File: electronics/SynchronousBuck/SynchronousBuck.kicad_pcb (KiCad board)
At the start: 4 copper layers, 90 x 81 mm, 58 parts, among them J101 Conn_01x02, J102 Conn_01x04_Male, J103 Conn_01x02, J104 Conn_01x02, Q101 BSC070N10NS5, Q102 BSC067N06LS3G, U101 LM5116MH

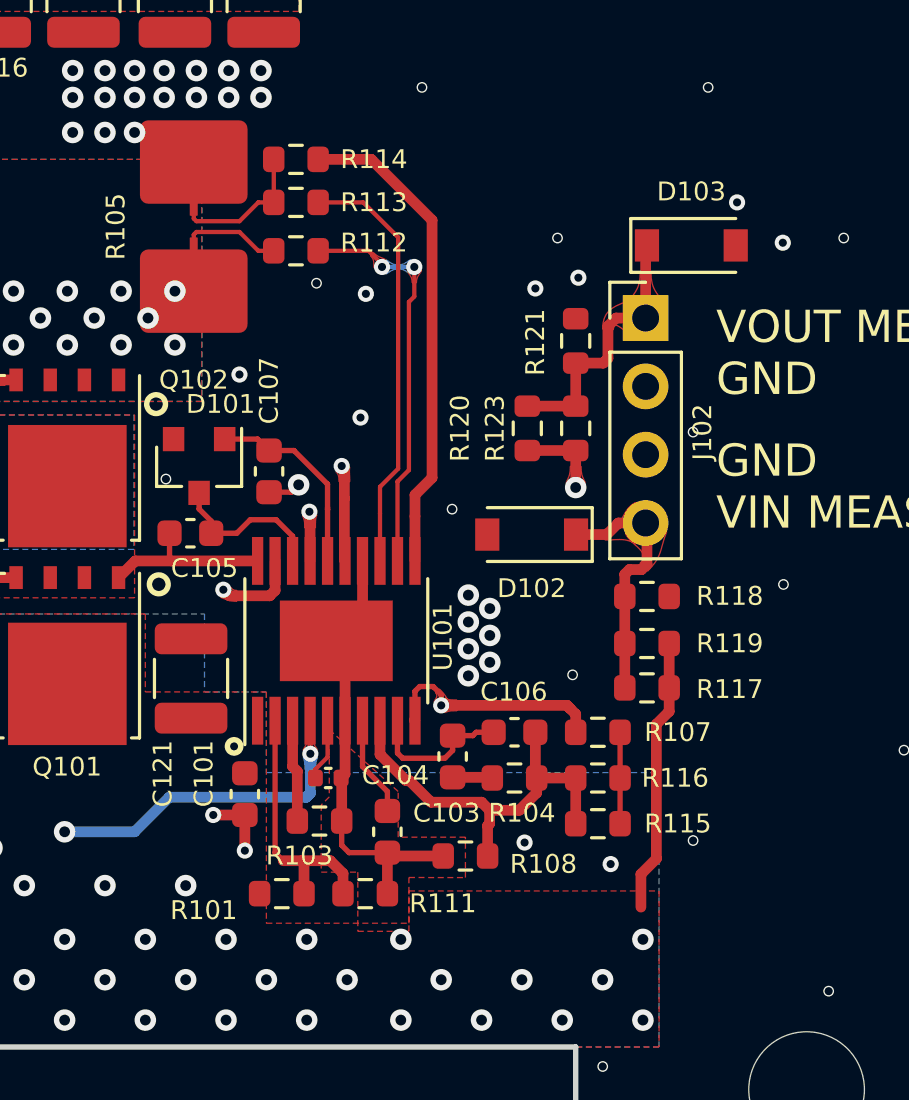
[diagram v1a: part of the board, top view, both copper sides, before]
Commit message: BOM optimization for JLCPcb assembly
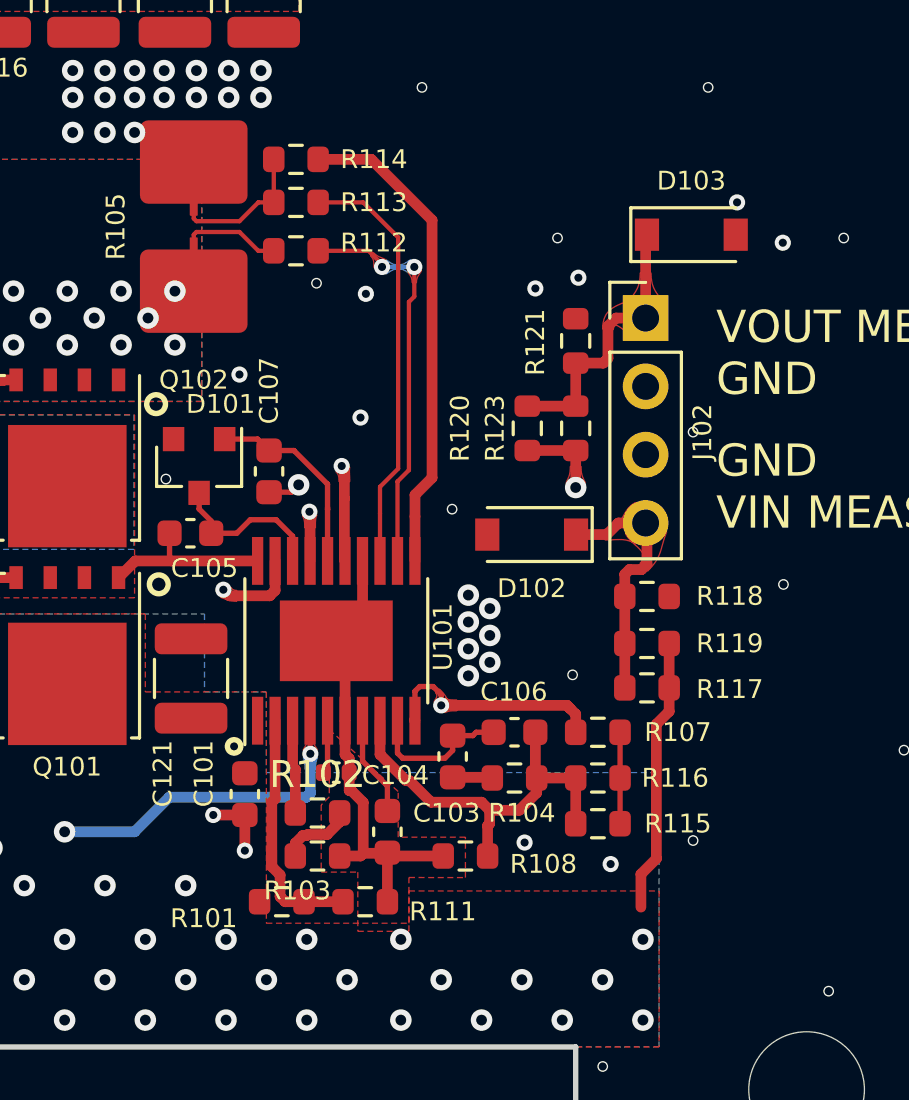
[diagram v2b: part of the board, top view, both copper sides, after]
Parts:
- added R102: 820, Resistor_SMD:R_0603_1608Metric, F.Cu at (110.4, 118.3)
- R103: value 9k1 -> 8k2
- moved R103 1.30 mm to (110.4, 119.9)
- moved D103 0.40 mm to (124.3, 96.8)
- moved C102 0.36 mm to (111.1, 116.8)
- moved R101 0.30 mm to (109.1, 121.6)
- moved R111 0.30 mm to (112.2, 121.6)
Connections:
- R103 pad 1: Net-(R103-Pad1) -> Net-(R102-Pad2)
- U101 pad 3: Net-(R103-Pad1) -> Net-(R102-Pad1)
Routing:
- net Net-(R103-Pad1): track 3.80 -> 0.00 mm
- net Net-(R102-Pad1): track 0.00 -> 3.47 mm
- net Net-(R102-Pad2): track 0.00 -> 2.79 mm
- net GND: track 22.3 -> 23.0 mm

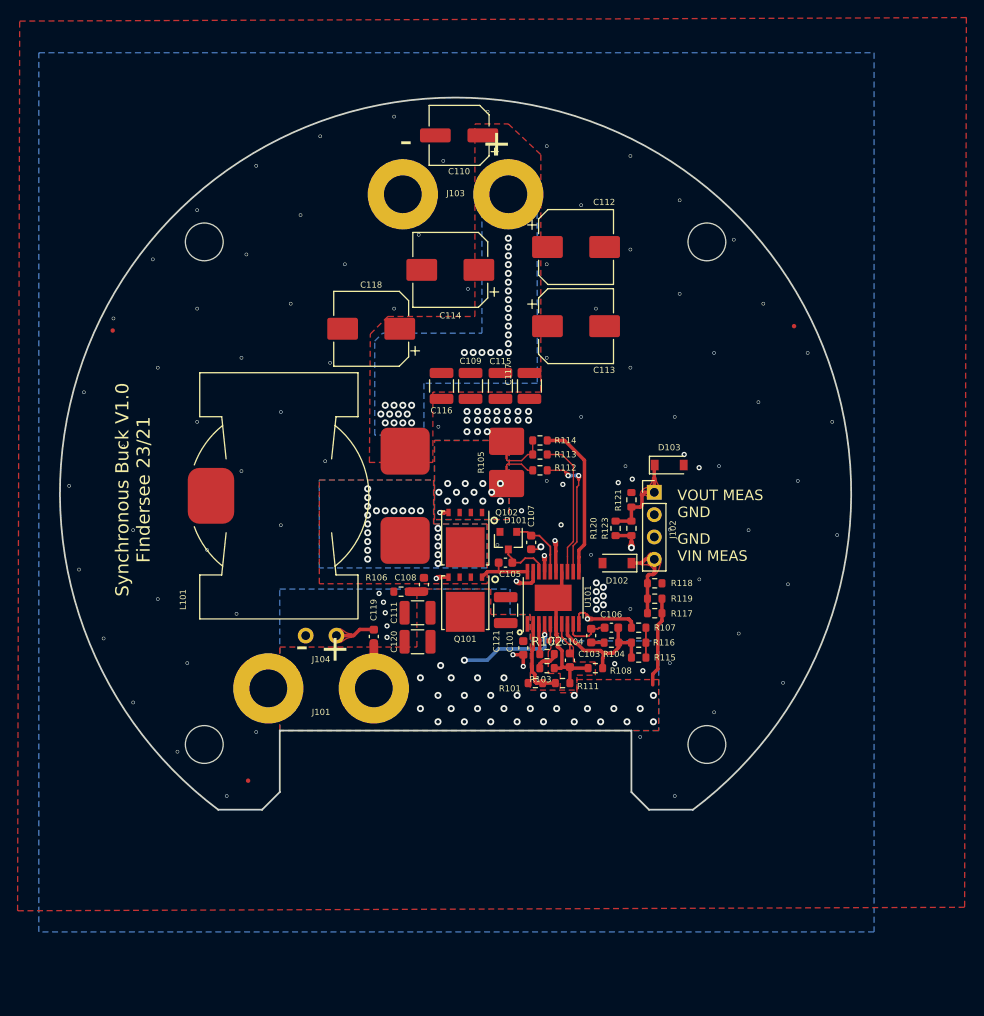
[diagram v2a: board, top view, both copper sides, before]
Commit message: Added Raspi Adapter Changed Buck Capacitors
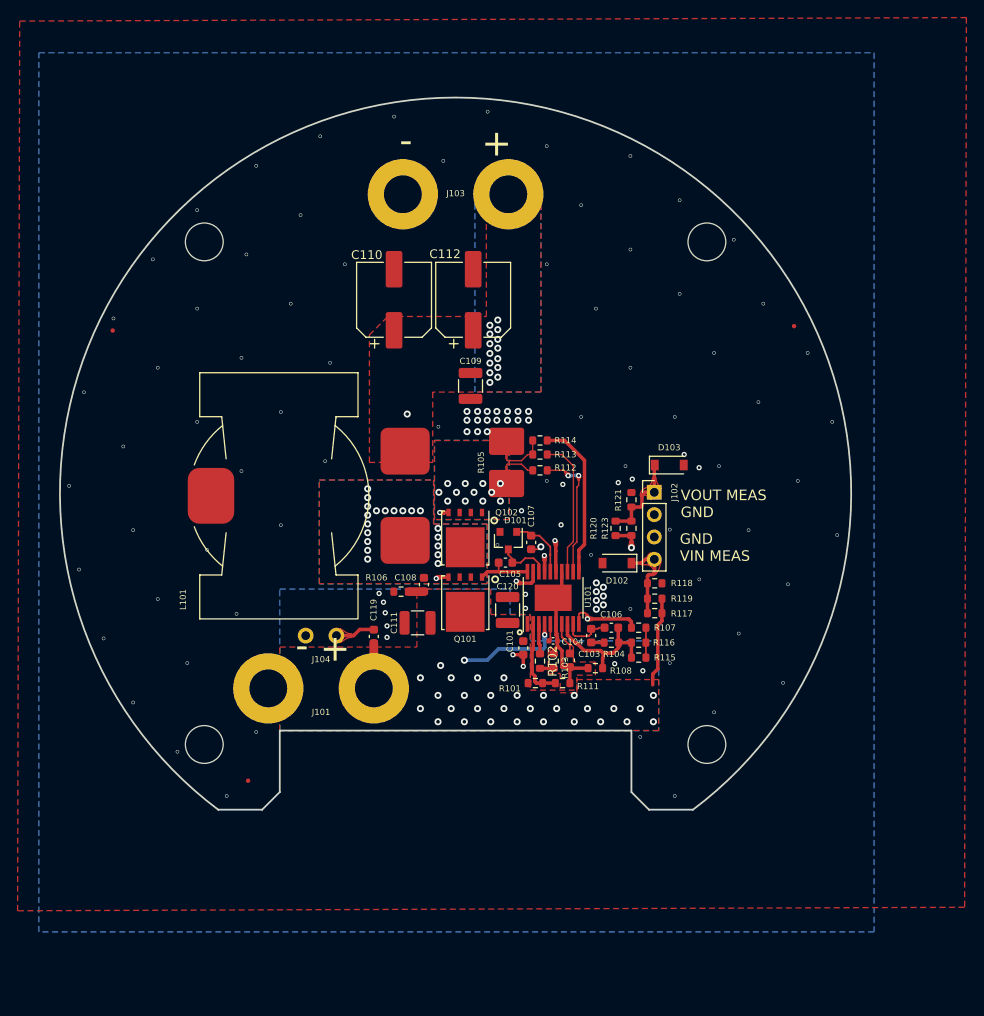
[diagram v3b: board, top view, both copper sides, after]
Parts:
- removed C113, C114, C118: 100u, Capacitor_SMD:CP_Elec_8x10
- removed C115, C116, C117, C121: 2u2, Capacitor_SMD:C_1210_3225Metric
- added G***: LOGO, SynchronousBuck:SubLogo, B.Cu at (83.6, 81.6)
- C110: value 100u -> 390u; footprint Capacitor_SMD:CP_Elec_6.3x7.7 -> Capacitor_SMD:CP_Elec_8x11.9
- C112: value 100u -> 390u; footprint Capacitor_SMD:CP_Elec_8x10 -> Capacitor_SMD:CP_Elec_8x11.9
- moved C110 20.1 mm to (93.0, 78.0), turned to 90 degrees
- moved C112 13.1 mm to (102.0, 78.0), turned to 90 degrees
- moved C120 10.9 mm to (105.9, 113.3), turned to 90 degrees
- moved C111 1.15 mm to (95.7, 114.8)
- moved R102 1.13 mm to (109.6, 119.1), turned to 270 degrees
- moved R103 1.10 mm to (111.2, 119.1), turned to 90 degrees
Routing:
- net Net-(R102-Pad2): track 2.79 -> 1.55 mm
- net GND: vias 116 -> 114
- net /VOUT: vias 34 -> 18
- added copper zone on In1.Cu, net VCC
- removed copper zone on In2.Cu, net /VOUT
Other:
- board text added: "SN:"

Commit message: Production Commit
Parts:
- added C113: C_Small, Capacitor_SMD:C_0603_1608Metric, F.Cu at (116.2, 119.3)
- added C114: C_Small, Capacitor_SMD:C_0603_1608Metric, F.Cu at (120.0, 116.1)
- C102: value 1.8p -> 680p
- R105: value 0R002 -> 0R005; footprint PCBDecals:R_2512_6332Metric_SHUNT -> PCBDecals:LR2512_3WLOW_SHUNT
- R112, R113: value 30k -> 100
- moved G*** 11.3 mm to (74.6, 88.4)
- moved R114 6.36 mm to (111.4, 100.1), turned to 270 degrees
- moved R113 4.52 mm to (109.0, 100.1), turned to 270 degrees
- moved R112 3.46 mm to (107.4, 100.1), turned to 270 degrees
- moved R116 2.41 mm to (120.1, 119.3), turned to 90 degrees
- moved R105 2.41 mm to (108.2, 96.3), turned to 0 degrees
- moved R115 2.40 mm to (118.5, 119.3), turned to 90 degrees
- moved R108 1.43 mm to (114.6, 119.3), turned to 270 degrees
- moved R107 1.11 mm to (121.6, 116.1), turned to 270 degrees
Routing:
- net /VOUT: track 108.7 -> 118.2 mm
- net Net-(R114-Pad2): track 18.1 -> 9.62 mm
- net Net-(R113-Pad2): track 15.8 -> 11.6 mm, vias 0 -> 2
- net Net-(R112-Pad2): track 15.1 -> 11.6 mm, vias 2 -> 0
- net Net-(R107-Pad2): track 3.40 -> 5.88 mm
- net GND: track 23.0 -> 24.3 mm, vias 114 -> 100
- net Net-(C106-Pad1): track 15.4 -> 14.6 mm
- net Net-(R105-Pad3): track 5.22 -> 5.79 mm

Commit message: Folder restructuring
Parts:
- removed G***: LOGO, SynchronousBuck:SubLogo
- removed R112, R113: 100, Resistor_SMD:R_0603_1608Metric
- added NT101: NetTie_2, NetTie:NetTie-2_SMD_Pad0.5mm, F.Cu at (102.7, 115.5)
- added Q103: BSC070N10NS5, Package_TO_SOT_SMD:TDSON-8-1, F.Cu at (89.0, 112.0)
- added Q104: BSC067N06LS3G, Package_TO_SOT_SMD:TDSON-8-1, F.Cu at (97.0, 104.0)
- J101, J103: footprint PCBDecals:2xM4 -> SynchronousBuck:2xM4
- J104: footprint Misc:1x2_3.5_pinHeader -> SynchronousBuck:1x2_3.5_pinHeader
- L101: footprint Misc:WE-HCF -> SynchronousBuck:WE-HCF
- R105: footprint PCBDecals:LR2512_3WLOW_SHUNT -> SynchronousBuck:R_2512_6332Metric_SHUNT
- moved FID102 81.3 mm to (59.4, 62.3), turned to 0 degrees
- moved FID103 59.0 mm to (116.7, 62.1), turned to 0 degrees
- moved FID101 42.8 mm to (116.8, 146.9), turned to 0 degrees
- moved R119 41.0 mm to (87.0, 132.2), turned to 0 degrees
- moved R117 39.4 mm to (87.0, 130.5), turned to 0 degrees
- moved R118 38.2 mm to (90.2, 130.5)
- moved R120 38.2 mm to (97.8, 71.8), turned to 0 degrees
- moved R123 37.4 mm to (97.8, 74.0), turned to 0 degrees
- moved D102 36.6 mm to (91.2, 132.5), turned to 0 degrees
- moved D103 33.4 mm to (102.2, 71.8)
- moved R121 32.5 mm to (101.5, 74.0), turned to 0 degrees
- moved C101 26.1 mm to (81.6, 116.5), turned to 0 degrees
- moved C120 26.1 mm to (81.8, 123.3), turned to 0 degrees
- moved J101 21.5 mm to (88.0, 143.4), turned to 180 degrees
- moved H101 21.4 mm to (113.2, 143.5), turned to 0 degrees
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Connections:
- net Net-(C106-Pad1) renamed /FB
- net Net-(Q102-Pad1) renamed /ShuntTop
- C102 pad 2: GND -> GNDA
- C103 pad 2: GND -> GNDA
- C113 pad 2: GND -> GNDA
- D101 pad 2: Net-(D101-Pad2) -> unconnected-(D101-Pad2)
- L101 pad 3: GND -> unconnected-(L101-Pad3)
- R103 pad 2: GND -> GNDA
- R108 pad 2: GND -> GNDA
- R111 pad 1: GND -> GNDA
- U101 pad 12: Net-(R112-Pad2) -> Net-(R105-Pad2)
- U101 pad 13: Net-(R113-Pad2) -> Net-(R105-Pad3)
- U101 pad 17: /VOUT -> GND
- U101 pad 6: GND -> GNDA
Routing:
- net /VOUT: track 118.2 -> 64.5 mm, vias 18 -> 2
- net Net-(D103-Pad1): track 10.1 -> 49.1 mm
- net Net-(D102-Pad1): track 9.50 -> 44.2 mm
- net VCC: track 27.8 -> 58.4 mm, vias 32 -> 23
- net GND: track 24.3 -> 0.00 mm, vias 100 -> 58
- net Net-(R105-Pad3): track 5.79 -> 24.6 mm, vias 0 -> 2
- net Net-(R105-Pad2): track 3.27 -> 18.7 mm, vias 0 -> 2
- net /HO: track 14.8 -> 27.3 mm, vias 2 -> 3
- net Net-(R112-Pad2): track 11.6 -> 0.00 mm
- net Net-(R113-Pad2): track 11.6 -> 0.00 mm, vias 2 -> 0
- net /SW: track 6.49 -> 17.1 mm, vias 20 -> 12
- net /LO: track 19.6 -> 25.4 mm, vias 2 -> 3
- net Net-(U101-Pad11): track 9.62 -> 4.22 mm
- net Net-(R107-Pad2): track 5.88 -> 3.16 mm
- net Net-(C119-Pad2): track 4.55 -> 2.22 mm
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- added copper zone on In1.Cu, net /ShuntTop
- added copper zone on In2.Cu, net /ShuntTop
- added copper zone on F.Cu, net GNDA
- removed copper zone on B.Cu, net /VOUT
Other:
- board size 90 x 81 mm -> 60 x 87 mm
- net class Default removed
- board text removed: "+ -"
- board text removed: "GND VIN MEAS"
- board text removed: "SN:"
- board text removed: "Synchronous Buck V1.0 Findersee 23/21"
- board text removed: "VOUT MEAS GND"
